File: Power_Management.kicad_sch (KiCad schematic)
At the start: 22 parts, among them J1 BATT, Q1 2N7002, SW1 POWER, U1 BQ24075RGT, U2 MAX17048

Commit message: feat(pcb): Version 0.2
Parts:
- removed R4: RLIM, Resistor_SMD:R_0603_1608Metric, symbol Device:R_Small
- C1, C4, C7: value 4.7uF -> (none); footprint Capacitor_SMD:C_0603_1608Metric -> (none)
- C2, C5, C6: value 1uF -> (none); footprint Capacitor_SMD:C_0603_1608Metric -> (none)
- C3: value 100nF -> (none); footprint Capacitor_SMD:C_0603_1608Metric -> (none)
- D1: value CHG -> (none); footprint Athena54:LED_1206_3216Metric (Reversible) -> (none)
- F1: value 500mA -> (none); footprint Fuse:Fuse_0603_1608Metric -> (none)
- J1: value BATT -> (none); footprint Athena54:Battery Header -> (none)
- Q1: value 2N7002 -> (none); footprint Package_TO_SOT_SMD:SOT-23 -> (none)
- R1: value 100 -> (none); footprint Resistor_SMD:R_0603_1608Metric -> (none)
- R2: value 10K -> (none); footprint Resistor_SMD:R_0603_1608Metric -> (none)
- R3: value RTMR -> (none); footprint Resistor_SMD:R_0603_1608Metric -> (none)
- R4: renamed from R5; value RSET -> (none); footprint Resistor_SMD:R_0603_1608Metric -> (none)
- R5: renamed from R6; value 100K -> (none); footprint Resistor_SMD:R_0603_1608Metric -> (none)
- R6: renamed from R7; value 10K -> (none); footprint Resistor_SMD:R_0603_1608Metric -> (none)
- R7: renamed from R8; value 1K5 -> (none); footprint Resistor_SMD:R_0603_1608Metric -> (none)
- SW1: value POWER -> (none); footprint Athena54:SW_SPDT_PCM12 (Reversible) -> (none)
- U1: value BQ24075RGT -> (none); footprint Package_DFN_QFN:VQFN-16-1EP_3x3mm_P0.5mm_EP1.6x1.6mm -> (none)
- U2: value MAX17048 -> (none); footprint Package_DFN_QFN:TDFN-8-1EP_2x2mm_P0.5mm_EP0.8x1.2mm -> (none)
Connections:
- net CHG: now also R7.1; no longer D1.1 (K)
- net VDDH: now also D1.2 (A); no longer R7.2
- net ILIM: no longer names the net of U1.12 (ILIM)
- new net: D1.1 (K), R7.2
- no-connect marks 1 -> 2
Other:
- note added: "Battery (500mAh)"
- note added: "Maximum Load Current: ILIM - ISET = 500mA - 296.7mA = 203.3mA"
- note added: "TMR: (10 * 48s/kOhm) * 15kOhm = 7200s = 2hr ILIM: 500mA (EN1 = 1, EN2 = 0) ISET: 890AOhm / 3kOhm = 0.2967A = 296.7mA (Fast Charge Current) TS: 10kOhm to GND = no temperature protection"
- note added: "nRF52840 - 50mA (RX & TX) USBLC6-2P6 - 150nA AO3407 - 5uA 2N7002 - 100nA MAX17048 - 23uA active, 3uA hibernate XC6220 - 50uA active, 8uA sleep"
- note removed: "Battery (402060, 500mAh)"
- note removed: "Maximum Load Current: ILIM - ISET = 500 - 100mA = 400mA (Moko MK08A takes less than 50mA for RX and TX)"
- note removed: "Moko MK08A - 50mA (RX & TX) USBLC6-2P6 - 150nA AO3407 - 5uA 2N7002 - 100nA MAX17048 - 23uA active, 3uA hibernate XC6220 - 50uA active, 8uA sleep"
- note removed: "TMR: (10 * 48s/kOhm) * 75kOhm = 36000s = 10hr ILIM: 500mA (EN1 = 1, EN2 = 0), 3.3kOhm as backup (1550AOhm/3.3kOhm = 0.46970A = 469.70mA) ISET: 890AOhm / 10kOhm = 0.089A = 89mA (Fast Charge Current) TS: 10kOhm to GND = no temperature protection"
- moved on the sheet: D1, R4, R6, R7

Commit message: feat(pcb): Version 0.2.1
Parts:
- C1, C4, C7: value (none) -> 4.7uF; footprint (none) -> Capacitor_SMD:C_0402_1005Metric
- C2, C5, C6: value (none) -> 1uF; footprint (none) -> Capacitor_SMD:C_0402_1005Metric
- C3: value (none) -> 100nF; footprint (none) -> Capacitor_SMD:C_0402_1005Metric
- D1: value (none) -> CHG; footprint (none) -> Athena54:LED_1206_3216Metric (Reversible)
- F1: value (none) -> 500mA; footprint (none) -> Fuse:Fuse_0603_1608Metric
- J1: value (none) -> BATT; footprint (none) -> Athena54:Battery Header
- Q1: value (none) -> 2N7002; footprint (none) -> Package_TO_SOT_SMD:SOT-23
- R1: value (none) -> 100; footprint (none) -> Resistor_SMD:R_0402_1005Metric
- R2, R6: value (none) -> 10K; footprint (none) -> Resistor_SMD:R_0402_1005Metric
- R3: value (none) -> RTMR; footprint (none) -> Resistor_SMD:R_0402_1005Metric
- R4: value (none) -> RSET; footprint (none) -> Resistor_SMD:R_0402_1005Metric
- R5: value (none) -> 100K; footprint (none) -> Resistor_SMD:R_0402_1005Metric
- R7: value (none) -> 1K5; footprint (none) -> Resistor_SMD:R_0402_1005Metric
- U1: value (none) -> BQ24075RGT; footprint (none) -> Package_DFN_QFN:VQFN-16-1EP_3x3mm_P0.5mm_EP1.6x1.6mm
- U2: value (none) -> MAX17048; footprint (none) -> Package_DFN_QFN:TDFN-8-1EP_2x2mm_P0.5mm_EP0.8x1.2mm

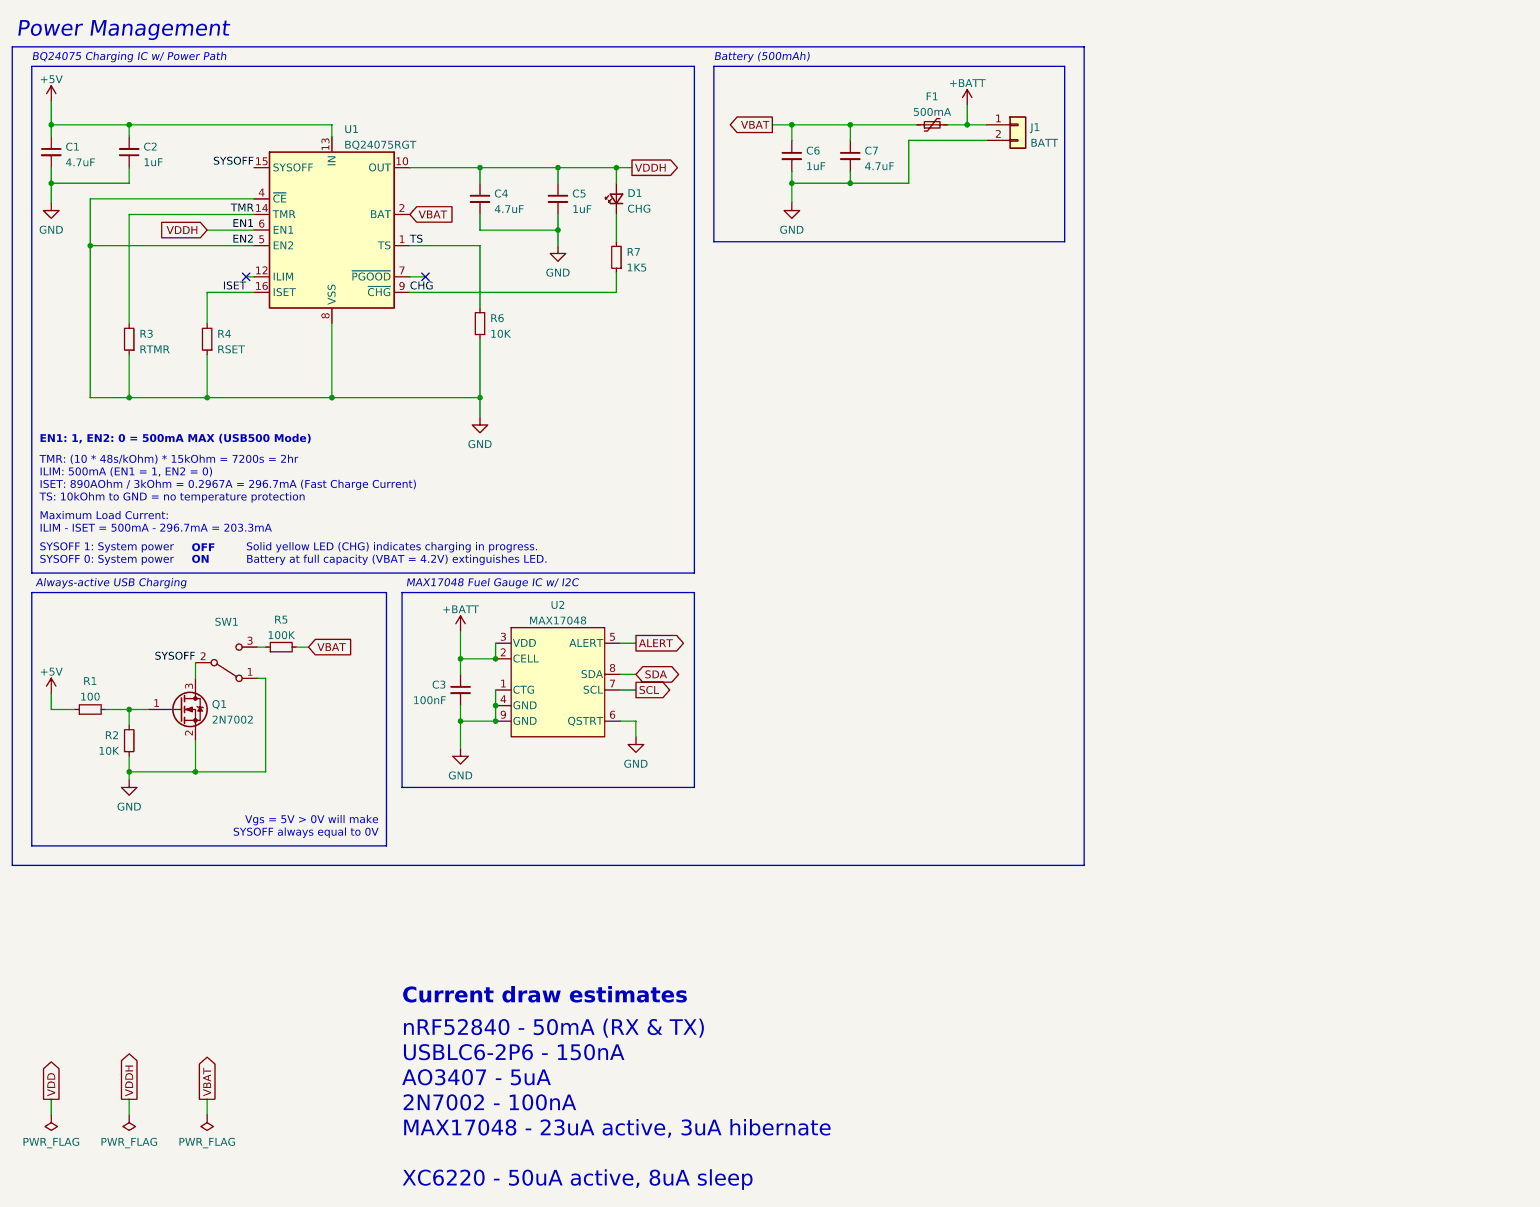
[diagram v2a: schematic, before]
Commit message: fix(schematic): Adjust charging parameters
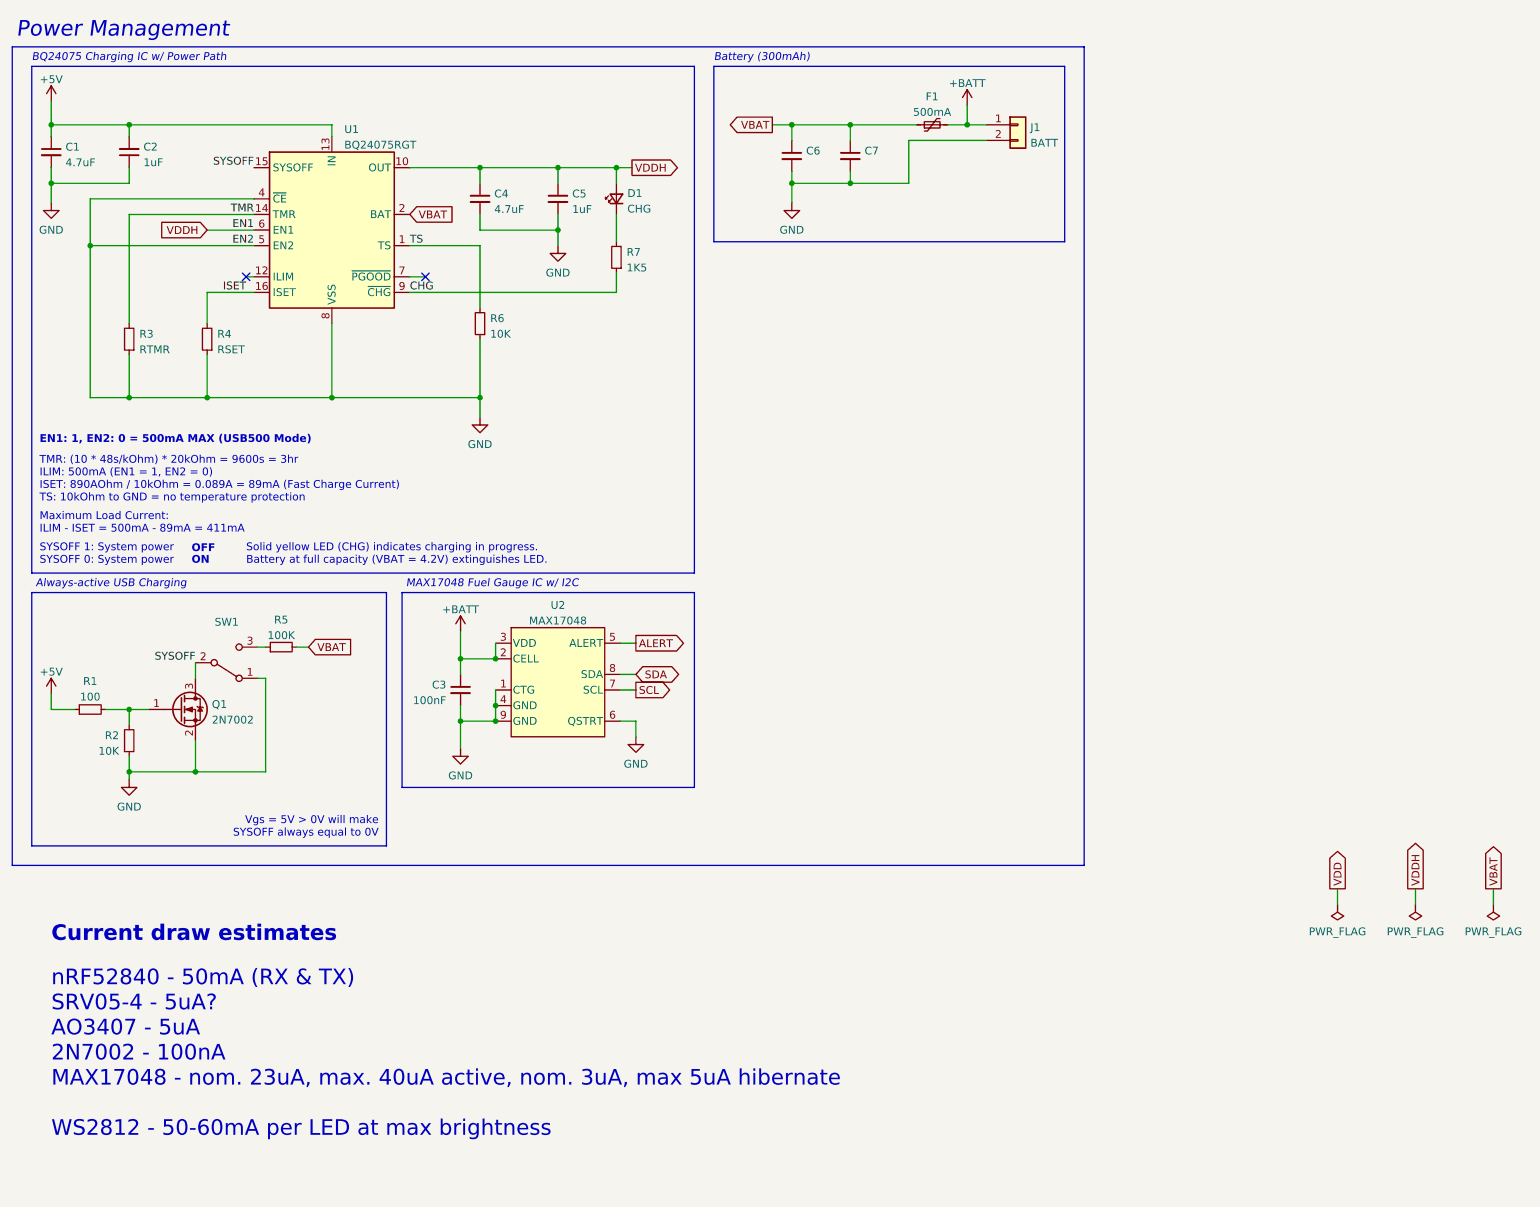
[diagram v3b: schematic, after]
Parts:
- C6: value 1uF -> (none); footprint Capacitor_SMD:C_0402_1005Metric -> (none)
- C7: value 4.7uF -> (none); footprint Capacitor_SMD:C_0402_1005Metric -> (none)
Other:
- note added: "Battery (300mAh)"
- note added: "Maximum Load Current: ILIM - ISET = 500mA - 89mA = 411mA"
- note added: "TMR: (10 * 48s/kOhm) * 20kOhm = 9600s = 3hr ILIM: 500mA (EN1 = 1, EN2 = 0) ISET: 890AOhm / 10kOhm = 0.089A = 89mA (Fast Charge Current) TS: 10kOhm to GND = no temperature protection"
- note added: "nRF52840 - 50mA (RX & TX) SRV05-4 - 5uA? AO3407 - 5uA 2N7002 - 100nA MAX17048 - nom. 23uA, max. 40uA active, nom. 3uA, max 5uA hibernate WS2812 - 50-60mA per LED at max brightness"
- note removed: "Battery (500mAh)"
- note removed: "Maximum Load Current: ILIM - ISET = 500mA - 296.7mA = 203.3mA"
- note removed: "TMR: (10 * 48s/kOhm) * 15kOhm = 7200s = 2hr ILIM: 500mA (EN1 = 1, EN2 = 0) ISET: 890AOhm / 3kOhm = 0.2967A = 296.7mA (Fast Charge Current) TS: 10kOhm to GND = no temperature protection"
- note removed: "nRF52840 - 50mA (RX & TX) USBLC6-2P6 - 150nA AO3407 - 5uA 2N7002 - 100nA MAX17048 - 23uA active, 3uA hibernate XC6220 - 50uA active, 8uA sleep"
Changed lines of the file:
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@@
     (stroke (width 0) (type default) (color 0 0 0 0))
   )
-  (wire (pts (xy 44.45 190.5) (xy 44.45 193.04))
+  (wire (pts (xy 254 156.21) (xy 254 158.75))
     (stroke (width 0) (type default) (color 0 0 0 0))
   )
@@
     (stroke (width 0) (type default) (color 0 0 0 0))
   )
-  (wire (pts (xy 19.05 190.5) (xy 19.05 193.04))
+  (wire (pts (xy 228.6 156.21) (xy 228.6 158.75))
     (stroke (width 0) (type default) (color 0 0 0 0))
   )
@@
     (stroke (width 0) (type default) (color 0 0 0 0))
   )
-  (wire (pts (xy 31.75 190.5) (xy 31.75 193.04))
+  (wire (pts (xy 241.3 156.21) (xy 241.3 158.75))
     (stroke (width 0) (type default) (color 0 0 0 0))
   )
@@
     (effects (font (size 1.27 1.27) (thickness 0.254) bold) (justify left bottom))
   )
-  (text "TMR: (10 * 48s/kOhm) * 15kOhm = 7200s = 2hr\nILIM: 500mA (EN1 = 1, EN2 = 0)\nISET: 890AOhm / 3kOhm = 0.2967A = 296.7mA (Fast Charge Current)\nTS: 10kOhm to GND = no temperature protection\n"
+  (text "TMR: (10 * 48s/kOhm) * 20kOhm = 9600s = 3hr\nILIM: 500mA (EN1 = 1, EN2 = 0)\nISET: 890AOhm / 10kOhm = 0.089A = 89mA (Fast Charge Current)\nTS: 10kOhm to GND = no temperature protection\n"
     (at 17.145 93.345 0)
     (effects (font (size 1.27 1.27)) (justify left bottom))
@@
     (effects (font (size 1.27 1.27) italic) (justify left bottom))
   )
-  (text "nRF52840 - 50mA (RX & TX)\nUSBLC6-2P6 - 150nA\nAO3407 - 5uA\n2N7002 - 100nA\nMAX17048 - 23uA active, 3uA hibernate\n\nXC6220 - 50uA active, 8uA sleep"
-    (at 76.2 205.105 0)
+  (text "nRF52840 - 50mA (RX & TX)\nSRV05-4 - 5uA?\nAO3407 - 5uA\n2N7002 - 100nA\nMAX17048 - nom. 23uA, max. 40uA active, nom. 3uA, max 5uA hibernate\n\nWS2812 - 50-60mA per LED at max brightness"
+    (at 19.05 196.85 0)
     (effects (font (size 2.54 2.54)) (justify left bottom))
   )
@@
     (effects (font (size 1.27 1.27) italic) (justify left bottom))
   )
-  (text "Maximum Load Current:\nILIM - ISET = 500mA - 296.7mA = 203.3mA"
+  (text "Maximum Load Current:\nILIM - ISET = 500mA - 89mA = 411mA"
     (at 17.145 98.425 0)
     (effects (font (size 1.27 1.27)) (justify left bottom))
   )
-  (text "Battery (500mAh)" (at 127 21.59 0)
+  (text "Battery (300mAh)" (at 127 21.59 0)
     (effects (font (size 1.27 1.27) italic) (justify left bottom))
   )
@@
     (effects (font (size 1.27 1.27)) (justify left bottom))
   )
-  (text "Current draw estimates" (at 76.2 175.26 0)
+  (text "Current draw estimates" (at 19.05 165.1 0)
     (effects (font (size 2.54 2.54) (thickness 0.254) bold) (justify left bottom))
   )
@@
     )
   )
-  (global_label "VDD" (shape output) (at 19.05 190.5 90) (fields_autoplaced)
+  (global_label "VDD" (shape output) (at 228.6 156.21 90) (fields_autoplaced)
     (effects (font (size 1.27 1.27)) (justify left))
-    (property "Intersheet References" "${INTERSHEET_REFS}" (id 0) (at 18.9706 184.4583 90)
+    (property "Intersheet References" "${INTERSHEET_REFS}" (id 0) (at 228.5206 150.1683 90)
       (effects (font (size 1.27 1.27)) (justify left) hide)
     )
@@
     )
   )
-  (global_label "VBAT" (shape output) (at 44.45 190.5 90) (fields_autoplaced)
+  (global_label "VBAT" (shape output) (at 254 156.21 90) (fields_autoplaced)
     (effects (font (size 1.27 1.27)) (justify left))
-    (property "Intersheet References" "${INTERSHEET_REFS}" (id 0) (at 44.3706 183.6721 90)
-      (effects (font (size 1.27 1.27)) (justify left) hide)
-    )
-  )
-  (global_label "VDDH" (shape output) (at 31.75 190.5 90) (fields_autoplaced)
+    (property "Intersheet References" "${INTERSHEET_REFS}" (id 0) (at 253.9206 149.3821 90)
+      (effects (font (size 1.27 1.27)) (justify left) hide)
+    )
+  )
+  (global_label "VDDH" (shape output) (at 241.3 156.21 90) (fields_autoplaced)
     (effects (font (size 1.27 1.27)) (justify left))
-    (property "Intersheet References" "${INTERSHEET_REFS}" (id 0) (at 31.6706 183.1279 90)
+    (property "Intersheet References" "${INTERSHEET_REFS}" (id 0) (at 241.2206 148.8379 90)
       (effects (font (size 1.27 1.27)) (justify left) hide)
     )
@@
     (pin "1")
   )
-  (symbol (lib_id "power:PWR_FLAG") (at 19.05 193.04 180) (unit 1)
-    (in_bom yes) (on_board yes) (fields_autoplaced)
-    (property "Reference" "#FLG0101" (id 0) (at 19.05 194.945 0)
-      (effects (font (size 1.27 1.27)) hide)
-    )
-    (property "Value" "PWR_FLAG" (id 1) (at 19.05 197.4834 0))
-    (property "Footprint" "" (id 2) (at 19.05 193.04 0)
-      (effects (font (size 1.27 1.27)) hide)
-    )
-    (property "Datasheet" "~" (id 3) (at 19.05 193.04 0)
+  (symbol (lib_id "power:PWR_FLAG") (at 228.6 158.75 180) (unit 1)
+    (in_bom yes) (on_board yes) (fields_autoplaced)
+    (property "Reference" "#FLG0101" (id 0) (at 228.6 160.655 0)
+      (effects (font (size 1.27 1.27)) hide)
+    )
+    (property "Value" "PWR_FLAG" (id 1) (at 228.6 163.1934 0))
+    (property "Footprint" "" (id 2) (at 228.6 158.75 0)
+      (effects (font (size 1.27 1.27)) hide)
+    )
+    (property "Datasheet" "~" (id 3) (at 228.6 158.75 0)
       (effects (font (size 1.27 1.27)) hide)
     )
@@
       (effects (font (size 1.27 1.27)) (justify left))
     )
-    (property "Value" "1uF" (id 1) (at 142.0241 38.5385 0)
-      (effects (font (size 1.27 1.27)) (justify left))
-    )
-    (property "Footprint" "Capacitor_SMD:C_0402_1005Metric" (id 2) (at 139.7 36.83 0)
+    (property "Value" "" (id 1) (at 142.0241 38.5385 0)
+      (effects (font (size 1.27 1.27)) (justify left))
+    )
+    (property "Footprint" "" (id 2) (at 139.7 36.83 0)
       (effects (font (size 1.27 1.27)) hide)
     )
@@
     (pin "1")
   )
-  (symbol (lib_id "power:PWR_FLAG") (at 44.45 193.04 180) (unit 1)
-    (in_bom yes) (on_board yes) (fields_autoplaced)
-    (property "Reference" "#FLG0107" (id 0) (at 44.45 194.945 0)
-      (effects (font (size 1.27 1.27)) hide)
-    )
-    (property "Value" "PWR_FLAG" (id 1) (at 44.45 197.4834 0))
-    (property "Footprint" "" (id 2) (at 44.45 193.04 0)
-      (effects (font (size 1.27 1.27)) hide)
-    )
-    (property "Datasheet" "~" (id 3) (at 44.45 193.04 0)
+  (symbol (lib_id "power:PWR_FLAG") (at 254 158.75 180) (unit 1)
+    (in_bom yes) (on_board yes) (fields_autoplaced)
+    (property "Reference" "#FLG0107" (id 0) (at 254 160.655 0)
+      (effects (font (size 1.27 1.27)) hide)
+    )
+    (property "Value" "PWR_FLAG" (id 1) (at 254 163.1934 0))
+    (property "Footprint" "" (id 2) (at 254 158.75 0)
+      (effects (font (size 1.27 1.27)) hide)
+    )
+    (property "Datasheet" "~" (id 3) (at 254 158.75 0)
       (effects (font (size 1.27 1.27)) hide)
     )
@@
     (pin "1")
   )
-  (symbol (lib_id "power:PWR_FLAG") (at 31.75 193.04 180) (unit 1)
-    (in_bom yes) (on_board yes) (fields_autoplaced)
-    (property "Reference" "#FLG0104" (id 0) (at 31.75 194.945 0)
-      (effects (font (size 1.27 1.27)) hide)
-    )
-    (property "Value" "PWR_FLAG" (id 1) (at 31.75 197.4834 0))
-    (property "Footprint" "" (id 2) (at 31.75 193.04 0)
-      (effects (font (size 1.27 1.27)) hide)
-    )
-    (property "Datasheet" "~" (id 3) (at 31.75 193.04 0)
+  (symbol (lib_id "power:PWR_FLAG") (at 241.3 158.75 180) (unit 1)
+    (in_bom yes) (on_board yes) (fields_autoplaced)
+    (property "Reference" "#FLG0104" (id 0) (at 241.3 160.655 0)
+      (effects (font (size 1.27 1.27)) hide)
+    )
+    (property "Value" "PWR_FLAG" (id 1) (at 241.3 163.1934 0))
+    (property "Footprint" "" (id 2) (at 241.3 158.75 0)
+      (effects (font (size 1.27 1.27)) hide)
+    )
+    (property "Datasheet" "~" (id 3) (at 241.3 158.75 0)
       (effects (font (size 1.27 1.27)) hide)
     )
@@
       (effects (font (size 1.27 1.27)) (justify left))
     )
-    (property "Value" "4.7uF" (id 1) (at 151.5491 38.5385 0)
-      (effects (font (size 1.27 1.27)) (justify left))
-    )
-    (property "Footprint" "Capacitor_SMD:C_0402_1005Metric" (id 2) (at 149.225 36.83 0)
-      (effects (font (size 1.27 1.27)) hide)
-    )
+    (property "Value" "" (id 1) (at 151.5491 38.5385 0)
+      (effects (font (size 1.27 1.27)) (justify left))
+    )
+    (property "Footprint" "" (id 2) (at 149.225 36.83 0)
+      (effects (font (size 1.27 1.27)) hide)
+    )
